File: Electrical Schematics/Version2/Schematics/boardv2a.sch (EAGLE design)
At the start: 629 parts, among them IC1 MCP41HVX1ST, IC2 ADUM4160BRW, IC3 SE555D, IC5 74LVC1G04DBV, IC6 74LVC1G04DBV, IC7 4030D, K1 G5V-2, K2 CP1SA-12V, Q1 IRLML2060TRPBFBSS123LT1G, Q10 IRLML2060TRPBFBSS123LT1G, Q11 IRLML2060TRPBFBSS123LT1G, Q12 IRLML2060TRPBFBSS123LT1G, Q13 IRLML2060TRPBFBSS123LT1G, Q17 IRLML2060TRPBFBSS123LT1G, Q18 MOSFET-PCHANNEL, Q19 IRLML2060TRPBFBSS123LT1G, Q2 IRLML2060TRPBFBSS123LT1G, Q3 IRLML2060TRPBFBSS123LT1G, Q4 MOSFET-PCHANNEL, Q5 MOSFET-PCHANNEL, Q6 IRLML2060TRPBFBSS123LT1G, Q7 ASFL1, Q8 IRLML2060TRPBFBSS123LT1G, Q9 IRLML2060TRPBFBSS123LT1G, U1 CP2130-GM, U10 SN65HVDA100-Q1_D_8, U11 ADUM3442CRWZ, U12 ADUM3442CRWZ, U13 ADUM3442CRWZ, U14 ADUM3442CRWZ, U15 ADUM3442CRWZ, U16 ADUM3442CRWZ, U17 ADUM3442CRWZ, U18 LM1085_KTT_3, U19 ADUM3442CRWZ, U2 TMS570LS0432_PZ_100, U20 ADUM3442CRWZ, U3 LM1085_KTT_3, U4 LM1085_KTT_3, U5 LM1084_KTT_3, U6 TPS3514_D_14, U7 LM1085_KTT_3, U9 ADUM3442CRWZ, X4 5566-4

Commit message: fixed up fnr
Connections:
- net VOLTAGEJMP_+_TO_INPUT_VREG: now also K22.S
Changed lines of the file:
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@@
 <setting verticaltext="up"/>
 </settings>
-<grid distance="0.1" unitdist="inch" unit="inch" style="lines" multiple="1" display="no" altdistance="0.01" altunitdist="inch" altunit="inch"/>
+<grid distance="0.05" unitdist="inch" unit="inch" style="lines" multiple="1" display="no" altdistance="0.025" altunitdist="inch" altunit="inch"/>
 <layers>
 <layer number="1" name="Top" color="4" fill="1" visible="no" active="no"/>
@@
 <pinref part="JP88" gate="A" pin="2"/>
 <wire x1="15.24" y1="5.08" x2="22.86" y2="5.08" width="0.1524" layer="91"/>
+<pinref part="K2" gate="2" pin="S"/>
+<wire x1="-12.7" y1="110.49" x2="-6.35" y2="110.49" width="0.1524" layer="91"/>
+<wire x1="-6.35" y1="110.49" x2="-6.35" y2="99.06" width="0.1524" layer="91"/>
+<wire x1="-6.35" y1="99.06" x2="7.62" y2="99.06" width="0.1524" layer="91"/>
 </segment>
 </net>
@@
 <wire x1="7.62" y1="85.09" x2="-12.7" y2="85.09" width="0.1524" layer="91"/>
 <wire x1="-12.7" y1="85.09" x2="-12.7" y2="60.96" width="0.1524" layer="91"/>
-<wire x1="-12.7" y1="60.96" x2="-22.86" y2="60.96" width="0.1524" layer="91"/>
-<label x="-22.86" y="60.96" size="1.778" layer="95" rot="R180" xref="yes"/>
+<label x="-12.7" y="60.96" size="1.778" layer="95" xref="yes"/>
 <junction x="7.62" y="85.09"/>
 <wire x1="7.62" y1="85.09" x2="7.62" y2="81.28" width="0.1524" layer="91"/>

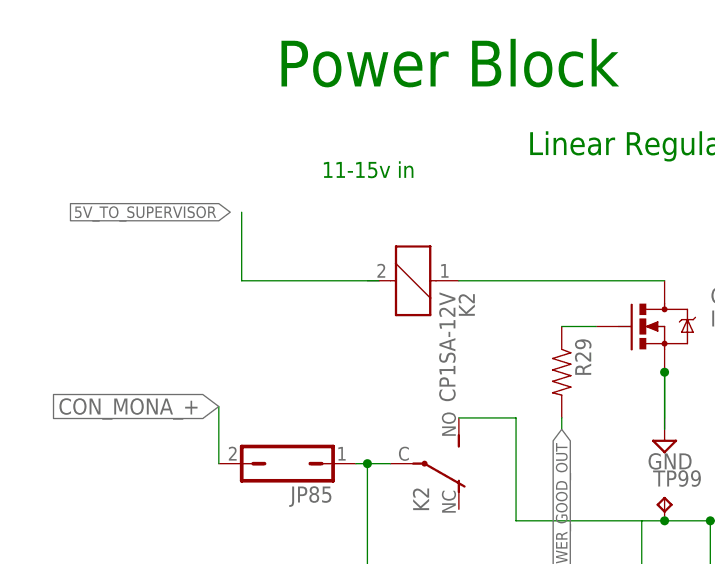
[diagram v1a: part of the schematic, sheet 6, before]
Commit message: cleaned up more routing
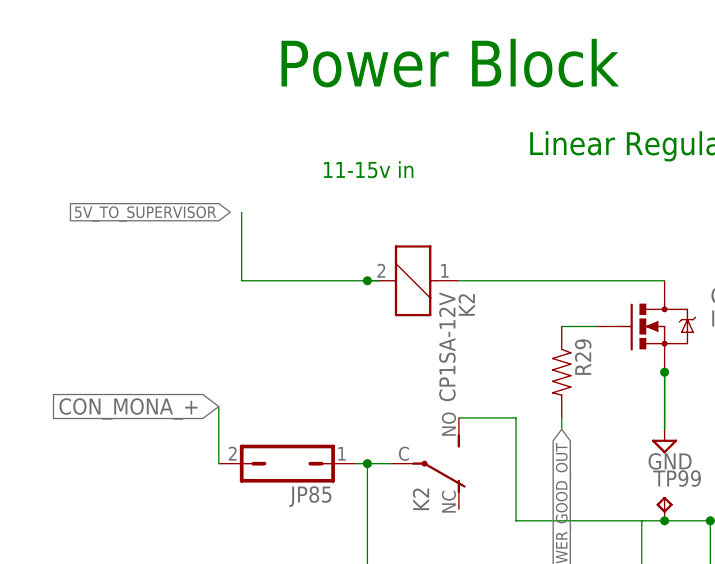
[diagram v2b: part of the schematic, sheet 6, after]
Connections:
- net 5V_TO_SUPERVISOR: now also K21.2
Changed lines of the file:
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@@
 <setting verticaltext="up"/>
 </settings>
-<grid distance="0.05" unitdist="inch" unit="inch" style="lines" multiple="1" display="no" altdistance="0.025" altunitdist="inch" altunit="inch"/>
+<grid distance="0.1" unitdist="inch" unit="inch" style="lines" multiple="1" display="no" altdistance="0.01" altunitdist="inch" altunit="inch"/>
 <layers>
 <layer number="1" name="Top" color="4" fill="1" visible="no" active="no"/>
@@
 </segment>
 <segment>
-<wire x1="-21.59" y1="125.73" x2="-36.83" y2="125.73" width="0.1524" layer="91"/>
+<wire x1="-21.59" y1="125.73" x2="-22.86" y2="125.73" width="0.1524" layer="91"/>
+<wire x1="-22.86" y1="125.73" x2="-36.83" y2="125.73" width="0.1524" layer="91"/>
 <wire x1="-36.83" y1="125.73" x2="-36.83" y2="133.35" width="0.1524" layer="91"/>
 <label x="-38.1" y="133.35" size="1.27" layer="95" rot="R180" xref="yes"/>
+<pinref part="K2" gate="1" pin="2"/>
+<junction x="-22.86" y="125.73"/>
 </segment>
 </net>

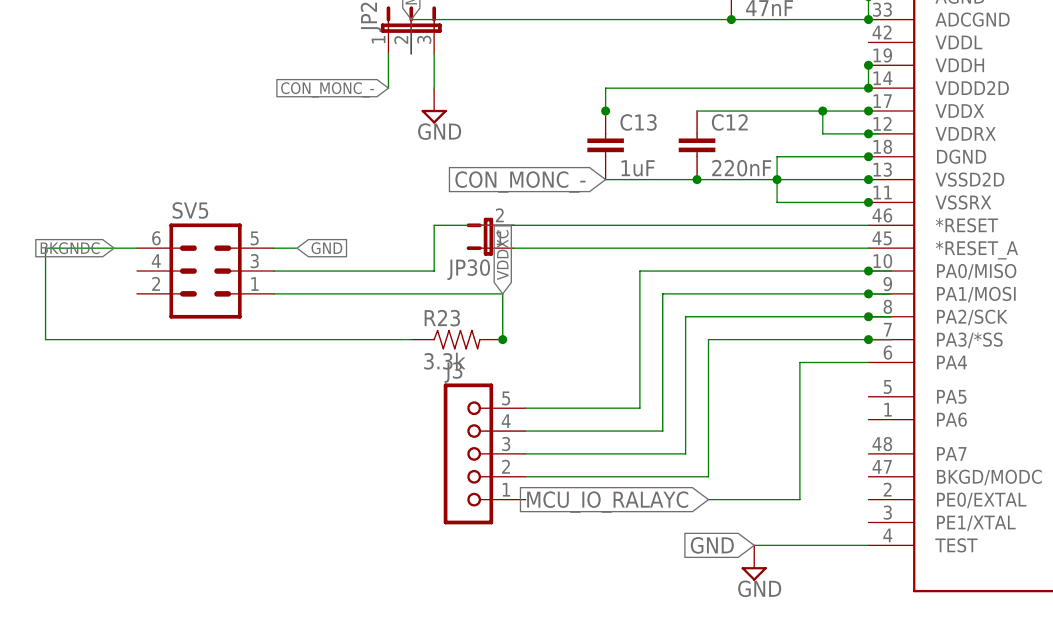
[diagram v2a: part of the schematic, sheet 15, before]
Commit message: updated battery monitor
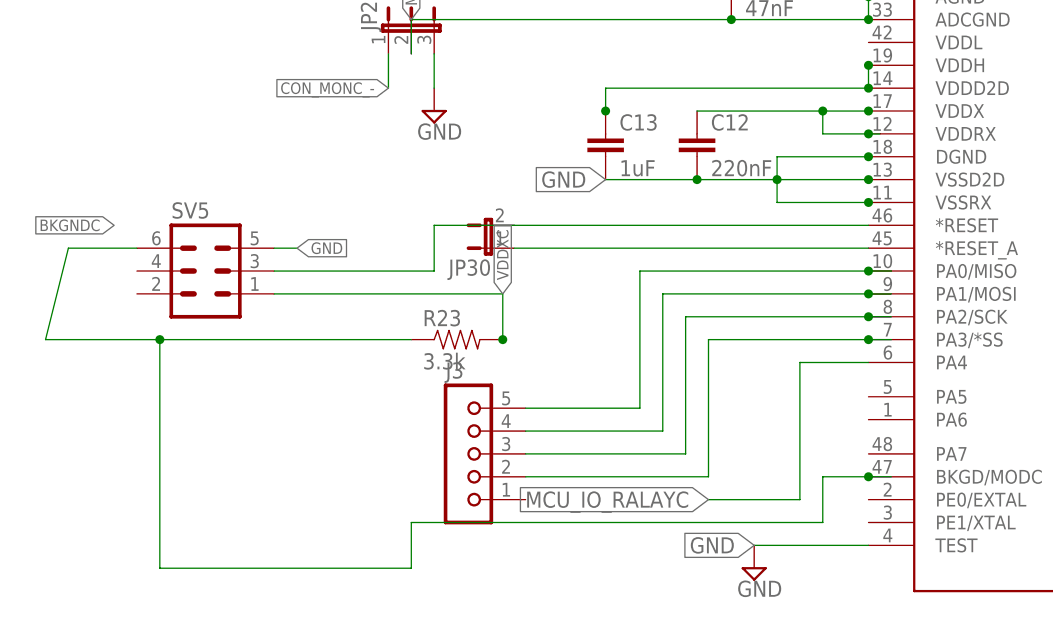
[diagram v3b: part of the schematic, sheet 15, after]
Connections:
- net BKGNDC: now also U$3.BKGD/MODC
- net CON_MONA_-: no longer C2.2, C3.2, U$1.DGND, U$1.VSSD2D, U$1.VSSRX
- net CON_MONB_-: no longer C7.2, C8.2, U$2.DGND, U$2.VSSD2D, U$2.VSSRX
- net CON_MONC_-: no longer C12.2, C13.2, U$3.DGND, U$3.VSSD2D, U$3.VSSRX
- net GND: now also C12.2, C13.2, C2.2, C3.2, C7.2, C8.2, U$1.DGND, U$1.VSSD2D, U$1.VSSRX, U$2.DGND, U$2.VSSD2D, U$2.VSSRX, U$3.DGND, U$3.VSSD2D, U$3.VSSRX
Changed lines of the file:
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@@
 <net name="CON_MONA_-" class="0">
-<segment>
-<pinref part="U$1" gate="A" pin="DGND"/>
-<wire x1="86.36" y1="76.2" x2="76.2" y2="76.2" width="0.1524" layer="91"/>
-<wire x1="76.2" y1="76.2" x2="76.2" y2="73.66" width="0.1524" layer="91"/>
-<wire x1="76.2" y1="73.66" x2="67.31" y2="73.66" width="0.1524" layer="91"/>
-<wire x1="67.31" y1="73.66" x2="57.15" y2="73.66" width="0.1524" layer="91"/>
-<pinref part="U$1" gate="A" pin="VSSD2D"/>
-<wire x1="86.36" y1="73.66" x2="76.2" y2="73.66" width="0.1524" layer="91"/>
-<pinref part="U$1" gate="A" pin="VSSRX"/>
-<wire x1="86.36" y1="71.12" x2="76.2" y2="71.12" width="0.1524" layer="91"/>
-<wire x1="76.2" y1="71.12" x2="76.2" y2="73.66" width="0.1524" layer="91"/>
-<pinref part="C2" gate="G$1" pin="2"/>
-<junction x="67.31" y="73.66"/>
-<junction x="86.36" y="76.2"/>
-<junction x="86.36" y="73.66"/>
-<junction x="86.36" y="71.12"/>
-<pinref part="C3" gate="G$1" pin="2"/>
-<label x="57.15" y="73.66" size="1.778" layer="95" rot="R180" xref="yes"/>
-<junction x="76.2" y="73.66"/>
-</segment>
 <segment>
 <pinref part="R2" gate="G$1" pin="2"/>
@@
 <wire x1="30.48" y1="66.04" x2="33.02" y2="66.04" width="0.1524" layer="91"/>
 <label x="33.02" y="66.04" size="1.27" layer="95" xref="yes"/>
+</segment>
+<segment>
+<pinref part="U$1" gate="A" pin="DGND"/>
+<wire x1="86.36" y1="76.2" x2="76.2" y2="76.2" width="0.1524" layer="91"/>
+<wire x1="76.2" y1="76.2" x2="76.2" y2="73.66" width="0.1524" layer="91"/>
+<wire x1="76.2" y1="73.66" x2="67.31" y2="73.66" width="0.1524" layer="91"/>
+<wire x1="67.31" y1="73.66" x2="57.15" y2="73.66" width="0.1524" layer="91"/>
+<pinref part="U$1" gate="A" pin="VSSD2D"/>
+<wire x1="86.36" y1="73.66" x2="76.2" y2="73.66" width="0.1524" layer="91"/>
+<pinref part="U$1" gate="A" pin="VSSRX"/>
+<wire x1="86.36" y1="71.12" x2="76.2" y2="71.12" width="0.1524" layer="91"/>
+<wire x1="76.2" y1="71.12" x2="76.2" y2="73.66" width="0.1524" layer="91"/>
+<pinref part="C2" gate="G$1" pin="2"/>
+<junction x="67.31" y="73.66"/>
+<junction x="86.36" y="76.2"/>
+<junction x="86.36" y="73.66"/>
+<junction x="86.36" y="71.12"/>
+<pinref part="C3" gate="G$1" pin="2"/>
+<label x="57.15" y="73.66" size="1.778" layer="95" rot="R180" xref="yes"/>
+<junction x="76.2" y="73.66"/>
 </segment>
 </net>
@@
 <label x="-55.88" y="76.2" size="1.27" layer="95" xref="yes"/>
 </segment>
-</net>
-<net name="MONB_AGND" class="0">
-<segment>
-<pinref part="C6" gate="G$1" pin="2"/>
-<pinref part="U$2" gate="A" pin="AGND"/>
-<wire x1="8.89" y1="104.14" x2="8.89" y2="101.6" width="0.1524" layer="91"/>
-<wire x1="8.89" y1="101.6" x2="-6.35" y2="101.6" width="0.1524" layer="91"/>
-<junction x="8.89" y="104.14"/>
-<pinref part="U$2" gate="A" pin="ADCGND"/>
-<junction x="8.89" y="101.6"/>
-<pinref part="JP24" gate="1" pin="2"/>
-<wire x1="-6.35" y1="101.6" x2="-41.91" y2="101.6" width="0.1524" layer="91"/>
-<wire x1="-41.91" y1="101.6" x2="-41.91" y2="97.79" width="0.1524" layer="91"/>
-<label x="-41.91" y="101.6" size="1.27" layer="95" rot="R90" xref="yes"/>
-<junction x="-6.35" y="101.6"/>
-</segment>
-</net>
-<net name="CON_MONB_-" class="0">
-<segment>
-<pinref part="JP24" gate="1" pin="1"/>
-<wire x1="-44.45" y1="97.79" x2="-44.45" y2="93.98" width="0.1524" layer="91"/>
-<label x="-44.45" y="93.98" size="1.27" layer="95" rot="R180" xref="yes"/>
-</segment>
 <segment>
 <pinref part="U$2" gate="A" pin="DGND"/>
@@
 <junction x="-1.27" y="83.82"/>
 </segment>
+</net>
+<net name="MONB_AGND" class="0">
+<segment>
+<pinref part="C6" gate="G$1" pin="2"/>
+<pinref part="U$2" gate="A" pin="AGND"/>
+<wire x1="8.89" y1="104.14" x2="8.89" y2="101.6" width="0.1524" layer="91"/>
+<wire x1="8.89" y1="101.6" x2="-6.35" y2="101.6" width="0.1524" layer="91"/>
+<junction x="8.89" y="104.14"/>
+<pinref part="U$2" gate="A" pin="ADCGND"/>
+<junction x="8.89" y="101.6"/>
+<pinref part="JP24" gate="1" pin="2"/>
+<wire x1="-6.35" y1="101.6" x2="-41.91" y2="101.6" width="0.1524" layer="91"/>
+<wire x1="-41.91" y1="101.6" x2="-41.91" y2="97.79" width="0.1524" layer="91"/>
+<label x="-41.91" y="101.6" size="1.27" layer="95" rot="R90" xref="yes"/>
+<junction x="-6.35" y="101.6"/>
+</segment>
+</net>
+<net name="CON_MONB_-" class="0">
+<segment>
+<pinref part="JP24" gate="1" pin="1"/>
+<wire x1="-44.45" y1="97.79" x2="-44.45" y2="93.98" width="0.1524" layer="91"/>
+<label x="-44.45" y="93.98" size="1.27" layer="95" rot="R180" xref="yes"/>
+</segment>
 <segment>
 <pinref part="R4" gate="G$1" pin="2"/>
@@
 <wire x1="-83.82" y1="66.04" x2="-43.18" y2="66.04" width="0.1524" layer="91"/>
 <pinref part="R22" gate="G$1" pin="1"/>
+<wire x1="10.16" y1="50.8" x2="2.54" y2="50.8" width="0.1524" layer="91"/>
+<wire x1="2.54" y1="50.8" x2="2.54" y2="45.72" width="0.1524" layer="91"/>
+<wire x1="2.54" y1="45.72" x2="-83.82" y2="45.72" width="0.1524" layer="91"/>
+<wire x1="-83.82" y1="45.72" x2="-83.82" y2="66.04" width="0.1524" layer="91"/>
+<junction x="10.16" y="50.8"/>
 </segment>
 </net>
@@
 <net name="CON_MONC_-" class="0">
 <segment>
-<pinref part="U$3" gate="A" pin="DGND"/>
-<wire x1="-15.24" y1="91.44" x2="-25.4" y2="91.44" width="0.1524" layer="91"/>
-<wire x1="-25.4" y1="91.44" x2="-25.4" y2="88.9" width="0.1524" layer="91"/>
-<wire x1="-25.4" y1="88.9" x2="-34.29" y2="88.9" width="0.1524" layer="91"/>
-<wire x1="-34.29" y1="88.9" x2="-44.45" y2="88.9" width="0.1524" layer="91"/>
-<pinref part="U$3" gate="A" pin="VSSD2D"/>
-<wire x1="-15.24" y1="88.9" x2="-25.4" y2="88.9" width="0.1524" layer="91"/>
-<pinref part="U$3" gate="A" pin="VSSRX"/>
-<wire x1="-15.24" y1="86.36" x2="-25.4" y2="86.36" width="0.1524" layer="91"/>
-<wire x1="-25.4" y1="86.36" x2="-25.4" y2="88.9" width="0.1524" layer="91"/>
-<pinref part="C12" gate="G$1" pin="2"/>
-<junction x="-34.29" y="88.9"/>
-<junction x="-15.24" y="91.44"/>
-<junction x="-15.24" y="88.9"/>
-<junction x="-15.24" y="86.36"/>
-<pinref part="C13" gate="G$1" pin="2"/>
-<label x="-44.45" y="88.9" size="1.778" layer="95" rot="R180" xref="yes"/>
-<junction x="-25.4" y="88.9"/>
-</segment>
-<segment>
 <pinref part="R8" gate="G$1" pin="2"/>
 <wire x1="58.42" y1="86.36" x2="58.42" y2="81.28" width="0.1524" layer="91"/>
@@
 <label x="-78.74" y="81.28" size="1.27" layer="95" xref="yes"/>
 </segment>
+<segment>
+<pinref part="U$3" gate="A" pin="DGND"/>
+<wire x1="-15.24" y1="91.44" x2="-25.4" y2="91.44" width="0.1524" layer="91"/>
+<wire x1="-25.4" y1="91.44" x2="-25.4" y2="88.9" width="0.1524" layer="91"/>
+<wire x1="-25.4" y1="88.9" x2="-34.29" y2="88.9" width="0.1524" layer="91"/>
+<wire x1="-34.29" y1="88.9" x2="-44.45" y2="88.9" width="0.1524" layer="91"/>
+<pinref part="U$3" gate="A" pin="VSSD2D"/>
+<wire x1="-15.24" y1="88.9" x2="-25.4" y2="88.9" width="0.1524" layer="91"/>
+<pinref part="U$3" gate="A" pin="VSSRX"/>
+<wire x1="-15.24" y1="86.36" x2="-25.4" y2="86.36" width="0.1524" layer="91"/>
+<wire x1="-25.4" y1="86.36" x2="-25.4" y2="88.9" width="0.1524" layer="91"/>
+<pinref part="C12" gate="G$1" pin="2"/>
+<junction x="-34.29" y="88.9"/>
+<junction x="-15.24" y="91.44"/>
+<junction x="-15.24" y="88.9"/>
+<junction x="-15.24" y="86.36"/>
+<pinref part="C13" gate="G$1" pin="2"/>
+<label x="-44.45" y="88.9" size="1.778" layer="95" rot="R180" xref="yes"/>
+<junction x="-25.4" y="88.9"/>
+</segment>
 </net>
 <net name="MONC_AGND" class="0">
@@
 <segment>
 <pinref part="SV5" gate="1" pin="6"/>
-<label x="-99.06" y="81.28" size="1.27" layer="95" rot="R180" xref="yes"/>
-<wire x1="-96.52" y1="81.28" x2="-106.68" y2="81.28" width="0.1524" layer="91"/>
-<wire x1="-106.68" y1="81.28" x2="-106.68" y2="71.12" width="0.1524" layer="91"/>
-<wire x1="-106.68" y1="71.12" x2="-66.04" y2="71.12" width="0.1524" layer="91"/>
+<label x="-99.06" y="83.82" size="1.27" layer="95" rot="R180" xref="yes"/>
+<wire x1="-96.52" y1="81.28" x2="-104.14" y2="81.28" width="0.1524" layer="91"/>
+<wire x1="-104.14" y1="81.28" x2="-106.68" y2="71.12" width="0.1524" layer="91"/>
+<wire x1="-106.68" y1="71.12" x2="-93.98" y2="71.12" width="0.1524" layer="91"/>
 <pinref part="R23" gate="G$1" pin="1"/>
-</segment>
-</net>
+<wire x1="-93.98" y1="71.12" x2="-66.04" y2="71.12" width="0.1524" layer="91"/>
+<wire x1="-12.7" y1="55.88" x2="-15.24" y2="55.88" width="0.1524" layer="91"/>
+<wire x1="-15.24" y1="55.88" x2="-20.32" y2="55.88" width="0.1524" layer="91"/>
+<wire x1="-20.32" y1="55.88" x2="-20.32" y2="50.8" width="0.1524" layer="91"/>
+<wire x1="-20.32" y1="50.8" x2="-66.04" y2="50.8" width="0.1524" layer="91"/>
+<wire x1="-66.04" y1="50.8" x2="-66.04" y2="45.72" width="0.1524" layer="91"/>
+<wire x1="-66.04" y1="45.72" x2="-93.98" y2="45.72" width="0.1524" layer="91"/>
+<wire x1="-93.98" y1="45.72" x2="-93.98" y2="71.12" width="0.1524" layer="91"/>
+<junction x="-93.98" y="71.12"/>
+<pinref part="U$3" gate="A" pin="BKGD/MODC"/>
+<junction x="-15.24" y="55.88"/>
+</segment>
+</net>

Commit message: cleaned  up more of the traces
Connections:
- removed net PP_3.3V_MODULARCONNECTOR: JP10.3, JP11.3, JP12.3, JP5.3, JP6.3, JP7.3, JP8.3, JP9.3
- removed net PP_5V_MODULARCONNECTOR: JP10.1, JP11.1, JP12.1, JP5.1, JP6.1, JP7.1, JP8.1, JP9.1
- net 3.3V_SUPERVISED: now also JP10.3, JP11.3, JP12.3, JP5.3, JP6.3, JP7.3, JP8.3, JP9.3; no longer C101.1, C103.1, C105.1, C91.1, C93.1, C95.1, C97.1, C99.1, U11.VDD1, U11.VE1, U12.VDD1, U12.VE1, U13.VDD1, U13.VE1, U14.VDD1, U14.VE1, U15.VDD1, U15.VE1, U16.VDD1, U16.VE1, U17.VDD1, U17.VE1, U9.VDD1, U9.VE1
- net 5V_SUPERVISED: now also JP10.1, JP11.1, JP12.1, JP5.1, JP6.1, JP7.1, JP8.1, JP9.1
- net PP_3.3V_FPGA: now also C101.1, C103.1, C105.1, C91.1, C93.1, C95.1, C97.1, C99.1, U11.VDD1, U11.VE1, U12.VDD1, U12.VE1, U13.VDD1, U13.VE1, U14.VDD1, U14.VE1, U15.VDD1, U15.VE1, U16.VDD1, U16.VE1, U17.VDD1, U17.VE1, U9.VDD1, U9.VE1

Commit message: almost finished saved now
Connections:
- net N$20: now also JP96.2
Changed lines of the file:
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@@
 </variantdefs>
 <classes>
-<class number="0" name="default" width="0.2032" drill="0.4064">
+<class number="0" name="default" width="0.2032" drill="0.254">
 <clearance class="0" value="0.1016"/>
 </class>
@@
 <wire x1="-24.13" y1="105.41" x2="-22.86" y2="105.41" width="0.1524" layer="91"/>
 <wire x1="-22.86" y1="105.41" x2="-20.32" y2="105.41" width="0.1524" layer="91"/>
-<wire x1="24.13" y1="58.42" x2="-22.86" y2="58.42" width="0.1524" layer="91"/>
+<wire x1="24.13" y1="58.42" x2="22.86" y2="58.42" width="0.1524" layer="91"/>
+<wire x1="22.86" y1="58.42" x2="-22.86" y2="58.42" width="0.1524" layer="91"/>
 <wire x1="-22.86" y1="58.42" x2="-22.86" y2="105.41" width="0.1524" layer="91"/>
 <junction x="-22.86" y="105.41"/>
+<pinref part="JP96" gate="A" pin="2"/>
+<junction x="22.86" y="58.42"/>
 </segment>
 </net>

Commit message: pushing final board
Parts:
- C52: device rcl:C-EUC0402 -> rcl:C-EUC0603
- U$8: value ACM3225-2P -> RFCMF1220100M3T; device shit:ACM3225-2P -> shit:RFCMF1220100M3T
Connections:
- removed net 3.3V_TEMP_PWR: JP100.2, JP101.2, JP102.2, JP97.2, JP98.2, JP99.2
- net MCU_+3.3V: now also JP100.2, JP101.2, JP102.2, JP97.2, JP98.2, JP99.2
